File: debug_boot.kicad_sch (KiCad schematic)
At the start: 11 parts, among them J3 Conn_ARM_JTAG_SWD_10, J4 Conn_01x03, J5 Conn_01x05, J6 Conn_01x03, J8 DE9_Pins

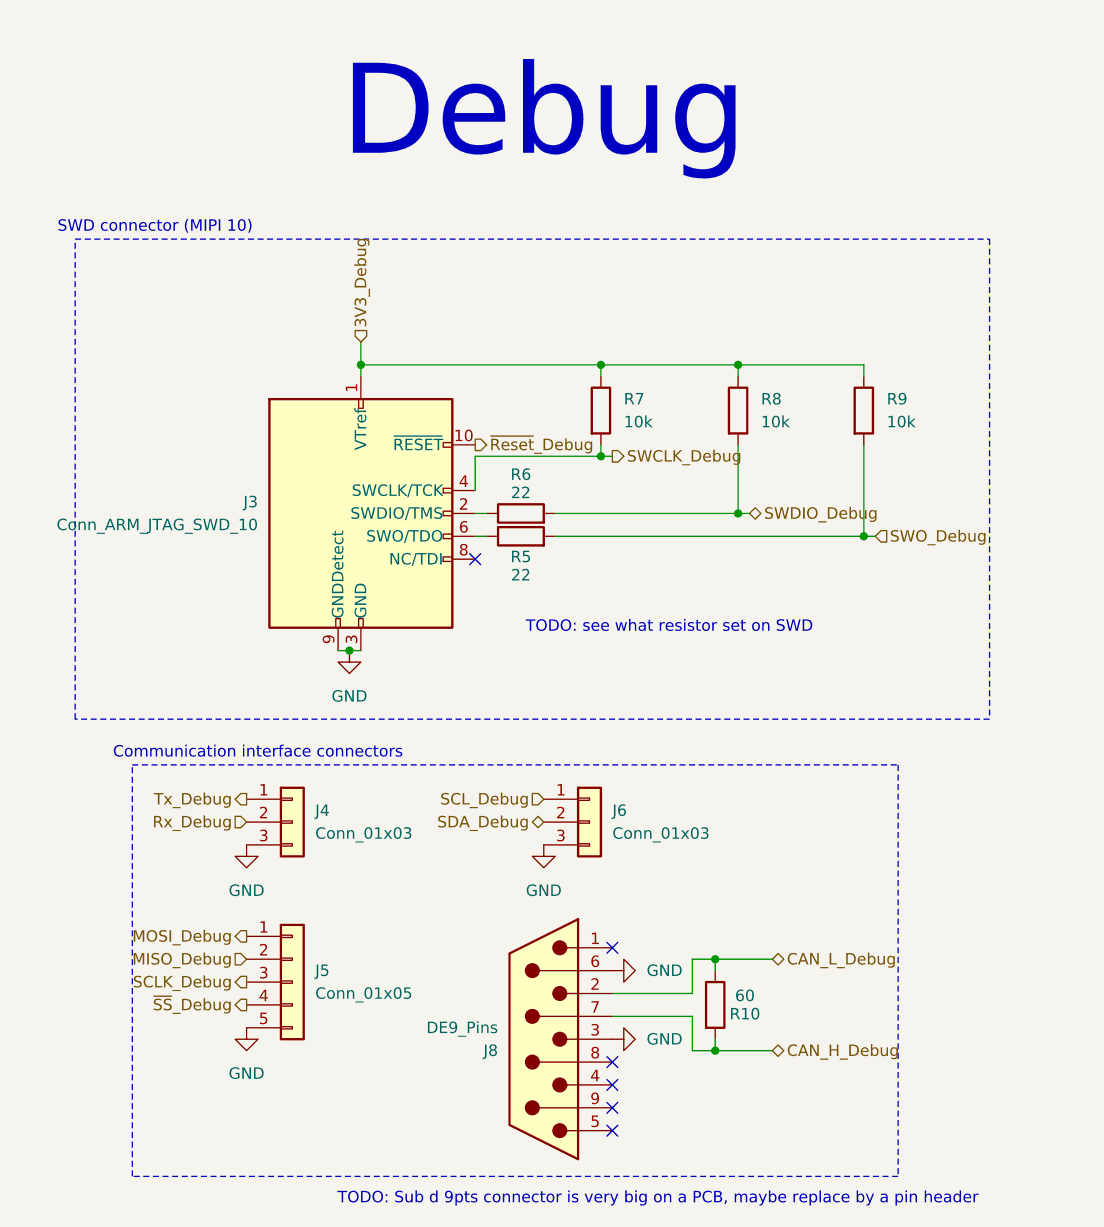
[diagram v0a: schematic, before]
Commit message: Fix some little warnings and refomat schematics files
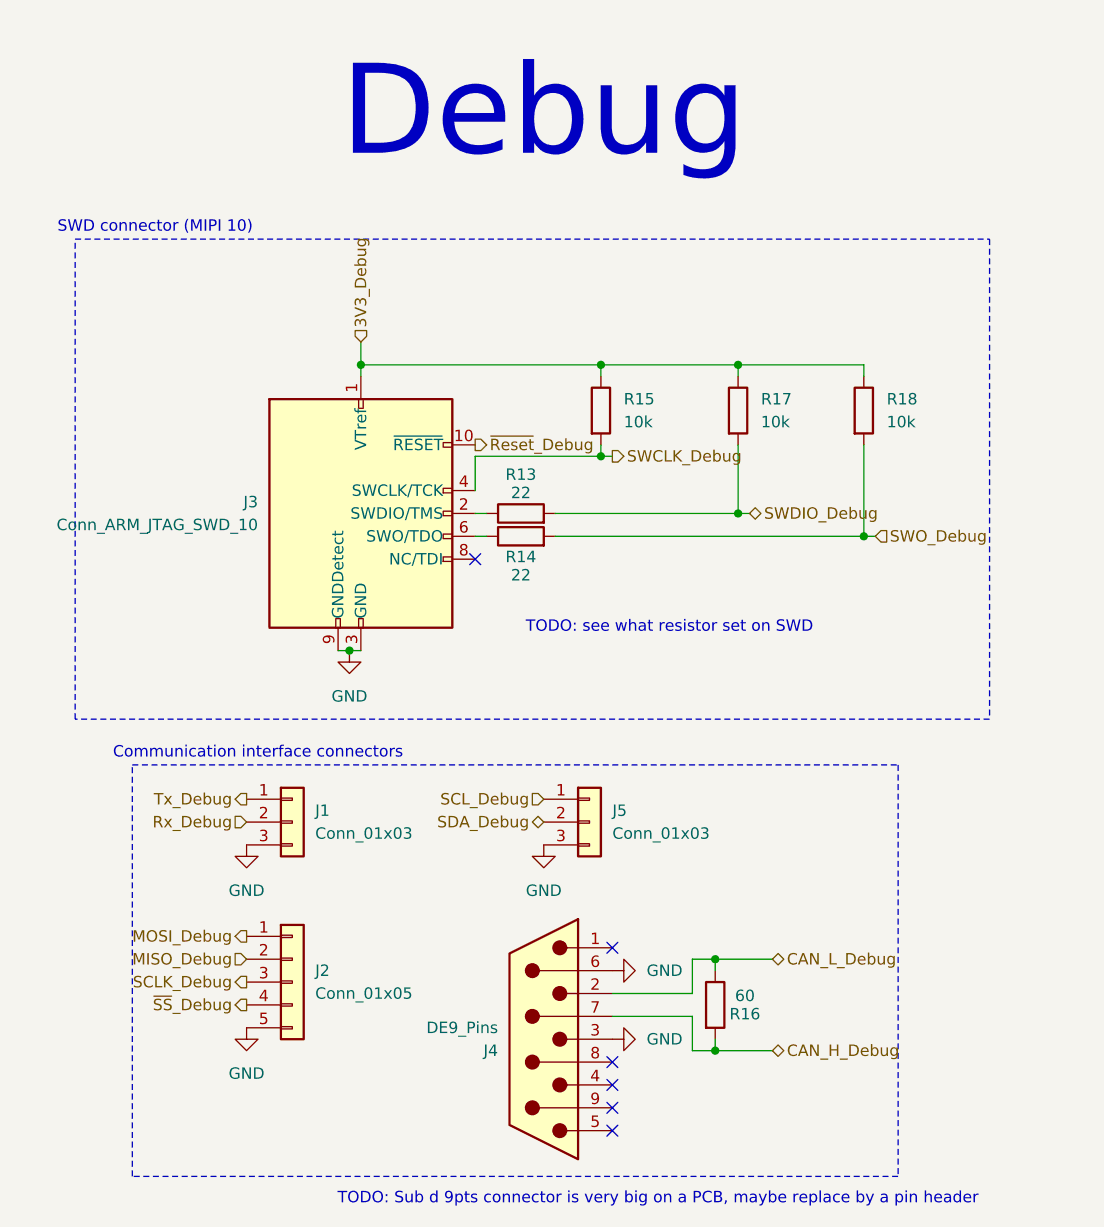
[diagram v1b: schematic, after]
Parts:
- renumbered J4 to J1, J5 to J2, J8 to J4, J6 to J5, R6 to R13, R5 to R14, R7 to R15, R10 to R16, R8 to R17, R9 to R18
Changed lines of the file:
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@@
 		(dnp no)
 		(fields_autoplaced yes)
-		(property "Reference" "#PWR034"
+		(property "Reference" "#PWR0121"
 			(at 166.37 120.65 0)
 			(effects
@@
 			(project "weather-station-poc"
 				(path "/38eb53bb-294e-46e4-ad59-fd355ca373b9/8a588a02-5ba4-4712-b770-7d9eb4e5d127"
-					(reference "#PWR034")
+					(reference "#PWR0121")
 					(unit 1)
 				)
@@
 		(on_board yes)
 		(dnp no)
-		(property "Reference" "R10"
+		(property "Reference" "R16"
 			(at 174.752 125.476 0)
 			(effects
@@
 			(project "weather-station-poc"
 				(path "/38eb53bb-294e-46e4-ad59-fd355ca373b9/8a588a02-5ba4-4712-b770-7d9eb4e5d127"
-					(reference "R10")
+					(reference "R16")
 					(unit 1)
 				)
@@
 		(dnp no)
 		(fields_autoplaced yes)
-		(property "Reference" "J6"
+		(property "Reference" "J5"
 			(at 160.02 102.8699 0)
 			(effects
@@
 			(project ""
 				(path "/38eb53bb-294e-46e4-ad59-fd355ca373b9/8a588a02-5ba4-4712-b770-7d9eb4e5d127"
-					(reference "J6")
+					(reference "J5")
 					(unit 1)
 				)
@@
 		(dnp no)
 		(fields_autoplaced yes)
-		(property "Reference" "#PWR035"
+		(property "Reference" "#PWR0122"
 			(at 166.37 128.27 0)
 			(effects
@@
 			(project "weather-station-poc"
 				(path "/38eb53bb-294e-46e4-ad59-fd355ca373b9/8a588a02-5ba4-4712-b770-7d9eb4e5d127"
-					(reference "#PWR035")
+					(reference "#PWR0122")
 					(unit 1)
 				)
@@
 		(on_board yes)
 		(dnp no)
-		(property "Reference" "R5"
+		(property "Reference" "R14"
 			(at 149.86 74.676 90)
 			(effects
@@
 			(project ""
 				(path "/38eb53bb-294e-46e4-ad59-fd355ca373b9/8a588a02-5ba4-4712-b770-7d9eb4e5d127"
-					(reference "R5")
+					(reference "R14")
 					(unit 1)
 				)
@@
 		(dnp no)
 		(fields_autoplaced yes)
-		(property "Reference" "R8"
+		(property "Reference" "R17"
 			(at 176.53 57.1499 0)
 			(effects
@@
 			(project "weather-station-poc"
 				(path "/38eb53bb-294e-46e4-ad59-fd355ca373b9/8a588a02-5ba4-4712-b770-7d9eb4e5d127"
-					(reference "R8")
+					(reference "R17")
 					(unit 1)
 				)
@@
 		(dnp no)
 		(fields_autoplaced yes)
-		(property "Reference" "J8"
+		(property "Reference" "J4"
 			(at 147.32 129.5401 0)
 			(effects
@@
 			(project ""
 				(path "/38eb53bb-294e-46e4-ad59-fd355ca373b9/8a588a02-5ba4-4712-b770-7d9eb4e5d127"
-					(reference "J8")
+					(reference "J4")
 					(unit 1)
 				)
@@
 		(on_board yes)
 		(dnp no)
-		(property "Reference" "R6"
+		(property "Reference" "R13"
 			(at 149.86 65.532 90)
 			(effects
@@
 			(project "weather-station-poc"
 				(path "/38eb53bb-294e-46e4-ad59-fd355ca373b9/8a588a02-5ba4-4712-b770-7d9eb4e5d127"
-					(reference "R6")
+					(reference "R13")
 					(unit 1)
 				)
@@
 		(dnp no)
 		(fields_autoplaced yes)
-		(property "Reference" "R7"
+		(property "Reference" "R15"
 			(at 161.29 57.1499 0)
 			(effects
@@
 			(project ""
 				(path "/38eb53bb-294e-46e4-ad59-fd355ca373b9/8a588a02-5ba4-4712-b770-7d9eb4e5d127"
-					(reference "R7")
+					(reference "R15")
 					(unit 1)
 				)
@@
 		(dnp no)
 		(fields_autoplaced yes)
-		(property "Reference" "#PWR032"
+		(property "Reference" "#PWR0118"
 			(at 119.38 133.35 0)
 			(effects
@@
 			(project "weather-station-poc"
 				(path "/38eb53bb-294e-46e4-ad59-fd355ca373b9/8a588a02-5ba4-4712-b770-7d9eb4e5d127"
-					(reference "#PWR032")
+					(reference "#PWR0118")
 					(unit 1)
 				)
@@
 		(dnp no)
 		(fields_autoplaced yes)
-		(property "Reference" "J5"
+		(property "Reference" "J2"
 			(at 127 120.6499 0)
 			(effects
@@
 			(project ""
 				(path "/38eb53bb-294e-46e4-ad59-fd355ca373b9/8a588a02-5ba4-4712-b770-7d9eb4e5d127"
-					(reference "J5")
+					(reference "J2")
 					(unit 1)
 				)
@@
 		(dnp no)
 		(fields_autoplaced yes)
-		(property "Reference" "#PWR033"
+		(property "Reference" "#PWR0120"
 			(at 152.4 113.03 0)
 			(effects
@@
 			(project "weather-station-poc"
 				(path "/38eb53bb-294e-46e4-ad59-fd355ca373b9/8a588a02-5ba4-4712-b770-7d9eb4e5d127"
-					(reference "#PWR033")
+					(reference "#PWR0120")
 					(unit 1)
 				)
@@
 		(dnp no)
 		(fields_autoplaced yes)
-		(property "Reference" "R9"
+		(property "Reference" "R18"
 			(at 190.5 57.1499 0)
 			(effects
@@
 			(project "weather-station-poc"
 				(path "/38eb53bb-294e-46e4-ad59-fd355ca373b9/8a588a02-5ba4-4712-b770-7d9eb4e5d127"
-					(reference "R9")
+					(reference "R18")
 					(unit 1)
 				)
@@
 		(dnp no)
 		(fields_autoplaced yes)
-		(property "Reference" "J4"
+		(property "Reference" "J1"
 			(at 127 102.8699 0)
 			(effects
@@
 			(project ""
 				(path "/38eb53bb-294e-46e4-ad59-fd355ca373b9/8a588a02-5ba4-4712-b770-7d9eb4e5d127"
-					(reference "J4")
+					(reference "J1")
 					(unit 1)
 				)
@@
 		(dnp no)
 		(fields_autoplaced yes)
-		(property "Reference" "#PWR031"
+		(property "Reference" "#PWR0117"
 			(at 119.38 113.03 0)
 			(effects
@@
 			(project ""
 				(path "/38eb53bb-294e-46e4-ad59-fd355ca373b9/8a588a02-5ba4-4712-b770-7d9eb4e5d127"
-					(reference "#PWR031")
+					(reference "#PWR0117")
 					(unit 1)
 				)
@@
 		(dnp no)
 		(fields_autoplaced yes)
-		(property "Reference" "#PWR029"
+		(property "Reference" "#PWR0119"
 			(at 130.81 91.44 0)
 			(effects
@@
 			(project ""
 				(path "/38eb53bb-294e-46e4-ad59-fd355ca373b9/8a588a02-5ba4-4712-b770-7d9eb4e5d127"
-					(reference "#PWR029")
-					(unit 1)
-				)
+					(reference "#PWR0119")
+					(unit 1)
+				)

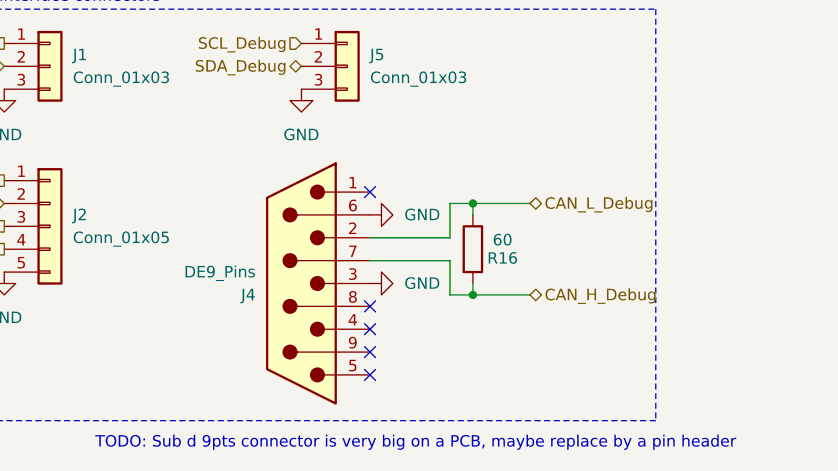
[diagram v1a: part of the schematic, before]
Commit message: Replace sub d 9 connectors by pin headers for CAN
Sub D 9 pts connectors are imposant on PCB
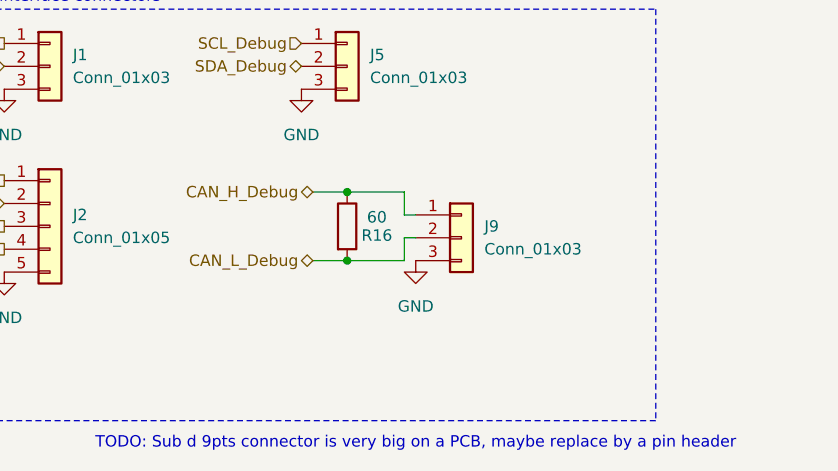
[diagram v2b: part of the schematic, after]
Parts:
- removed J4: DE9_Pins, symbol Connector:DE9_Pins
- added J9: Conn_01x03, symbol Connector_Generic:Conn_01x03
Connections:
- net CAN_H_Debug: now also R16.1, J9.1 (Pin_1); no longer R16.2
- net CAN_L_Debug: now also R16.2, J9.2 (Pin_2); no longer R16.1
- net GND: now also J9.3 (Pin_3)
- no-connect marks 6 -> 1
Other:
- moved on the sheet: R16

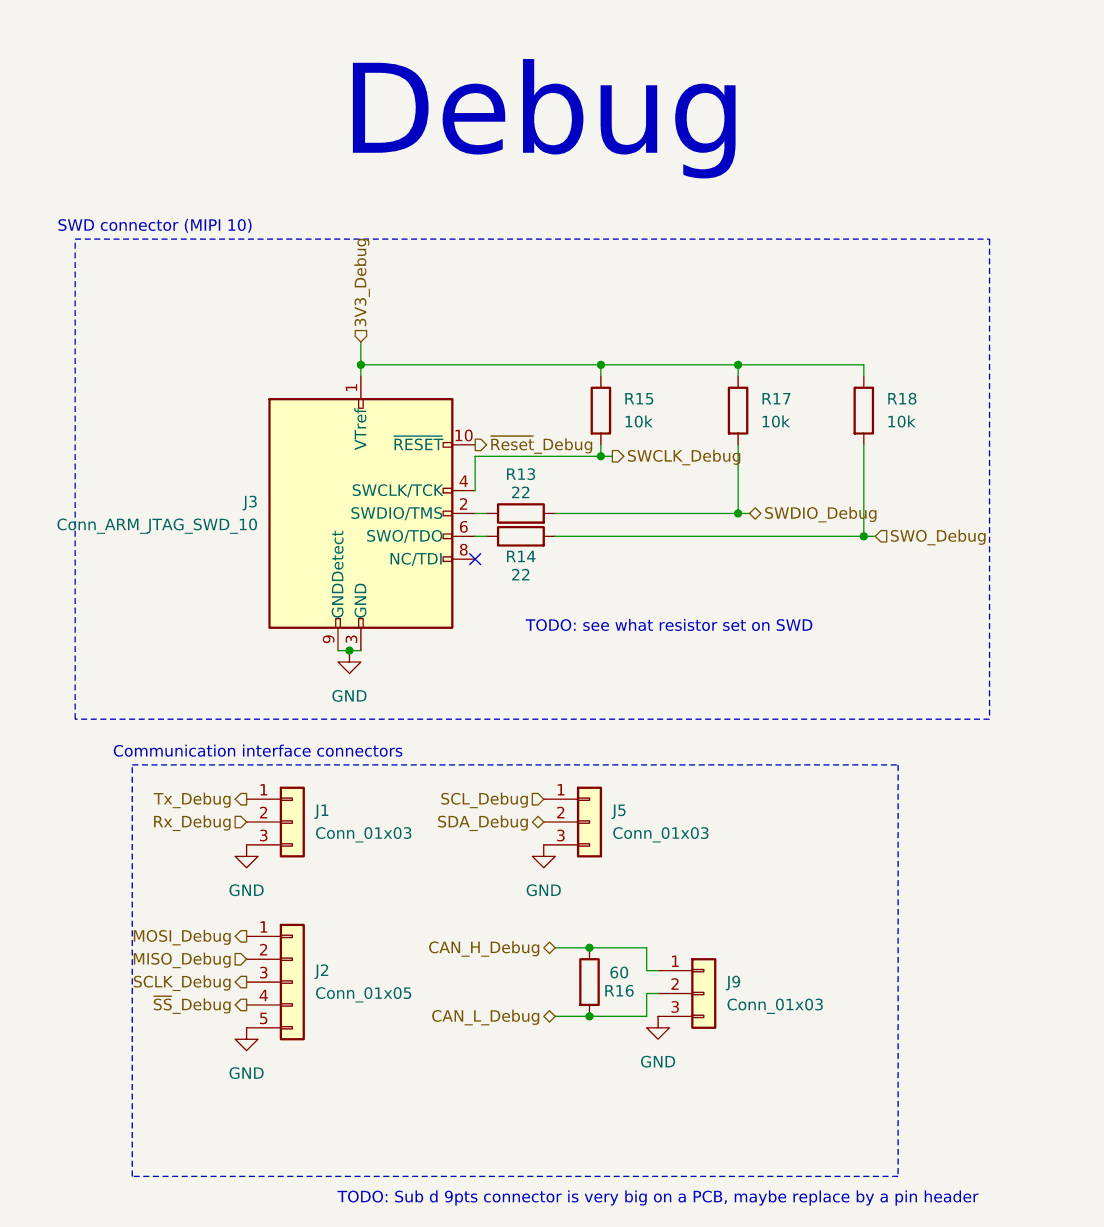
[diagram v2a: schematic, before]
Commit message: Add reference for debug connectors (pin headers)
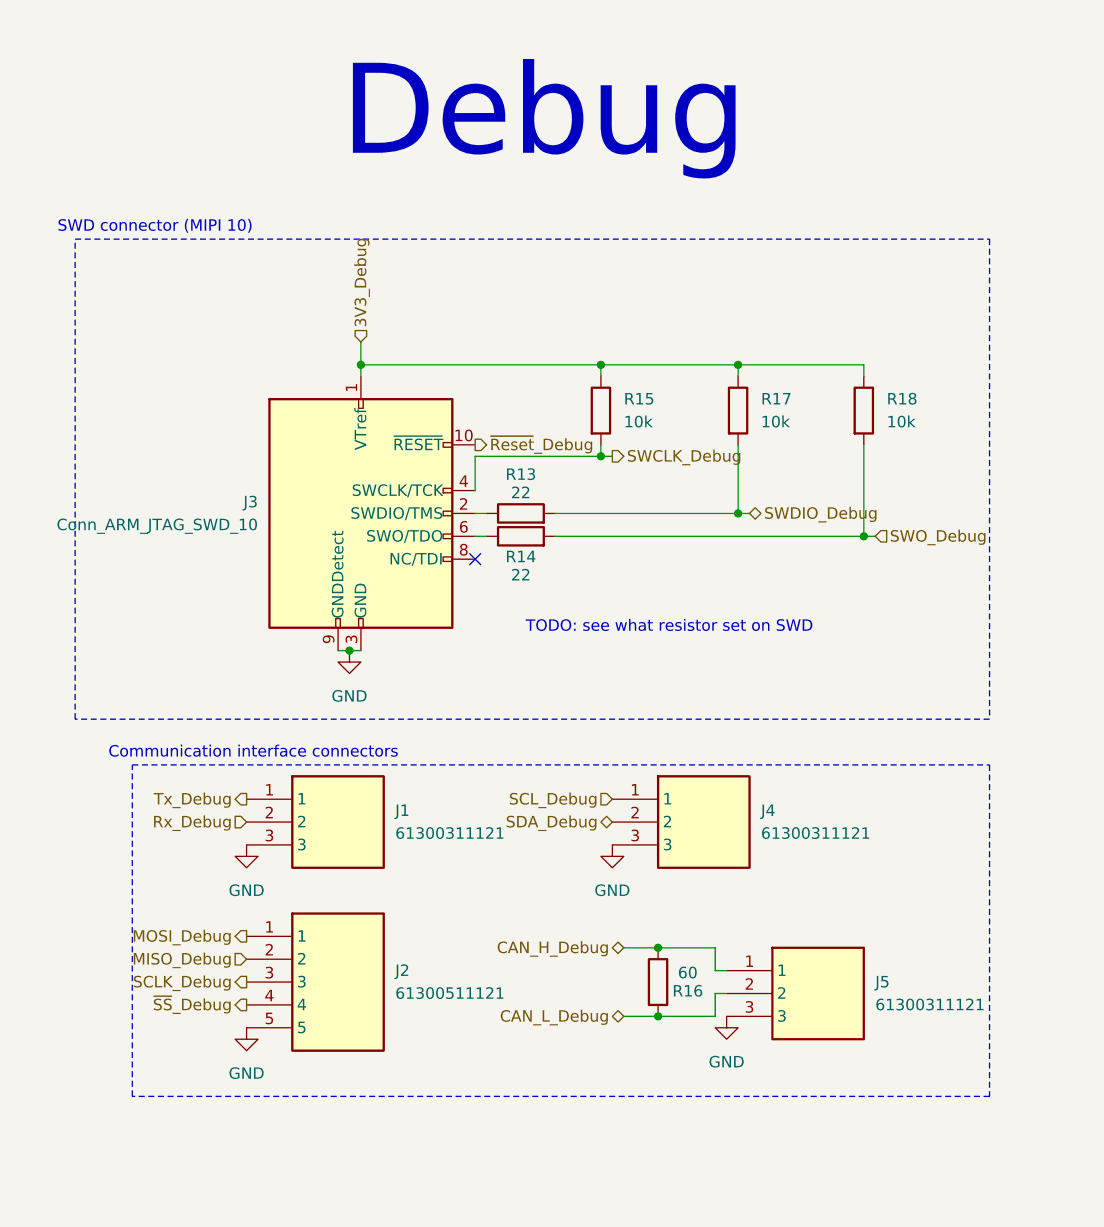
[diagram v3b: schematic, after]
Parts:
- removed J1, J5, J9: Conn_01x03, symbol Connector_Generic:Conn_01x03
- removed J2: Conn_01x05, symbol Connector_Generic:Conn_01x05
- added J1, J4, J5: 61300311121, weather-station-poc-fp:HDRV3W64P0X254_1X3_762X254X869P, symbol weather-station-poc-sym:61300311121
- added J2: 61300511121, weather-station-poc-fp:HDRV5W64P0X254_1X5_1270X254X854P, symbol weather-station-poc-sym:61300511121
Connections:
- net CAN_H_Debug: now also J5.1
- net CAN_L_Debug: now also J5.2
- net GND: now also J1.3, J2.5, J4.3, J5.3
- net MISO_Debug: now also J2.2
- net MOSI_Debug: now also J2.1
- net Rx_Debug: now also J1.2
- net SCLK_Debug: now also J2.3
- net SCL_Debug: now also J4.1
- net SDA_Debug: now also J4.2
- net Tx_Debug: now also J1.1
- net ~{SS}_Debug: now also J2.4
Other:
- note removed: "TODO: Sub d 9pts connector is very big on a PCB, maybe replace by a pin header"
- moved on the sheet: R16
